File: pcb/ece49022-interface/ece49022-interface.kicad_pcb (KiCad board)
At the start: 4 copper layers, 102 x 99 mm, 30 parts, among them J1 Conn_01x02_Pin, Q1 KSC1815, U4 NCP1117-3.3_SOT223, U5 TPS54202DDCT

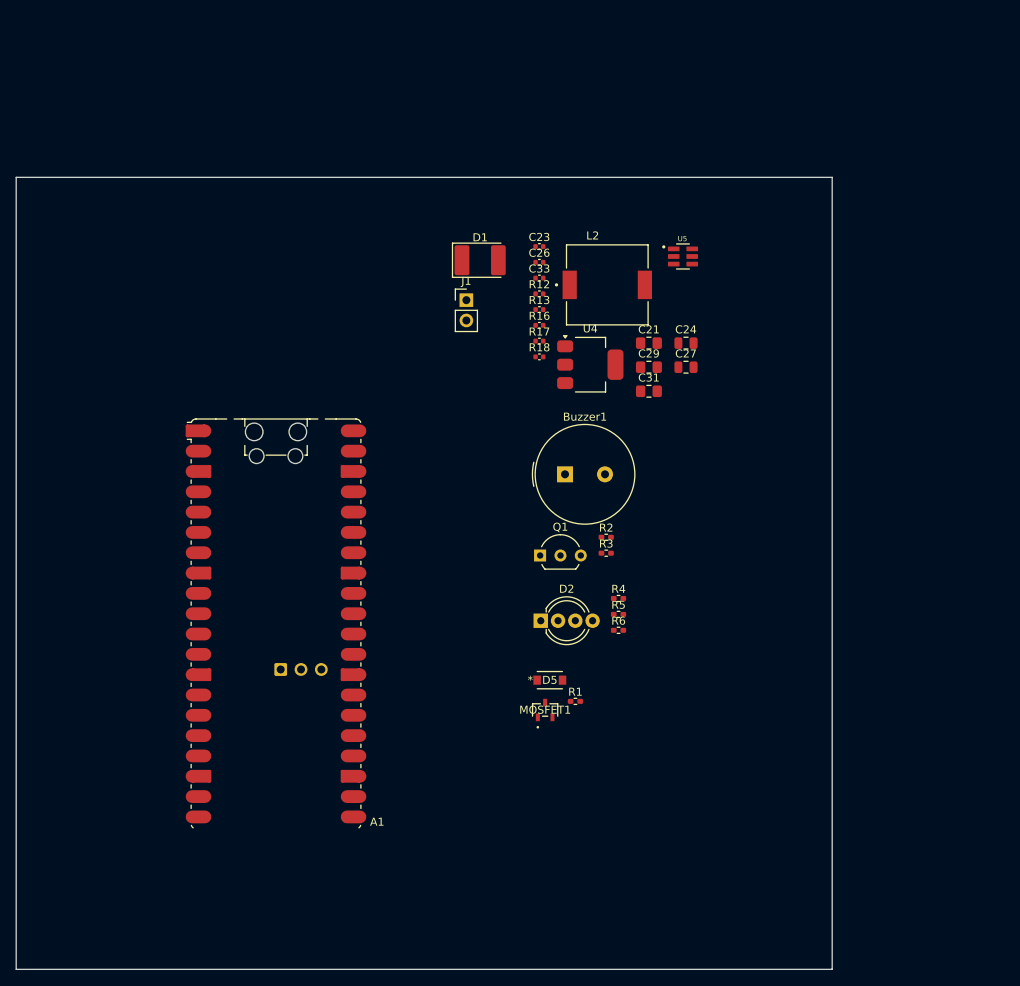
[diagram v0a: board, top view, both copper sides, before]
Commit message: Add pin connectors
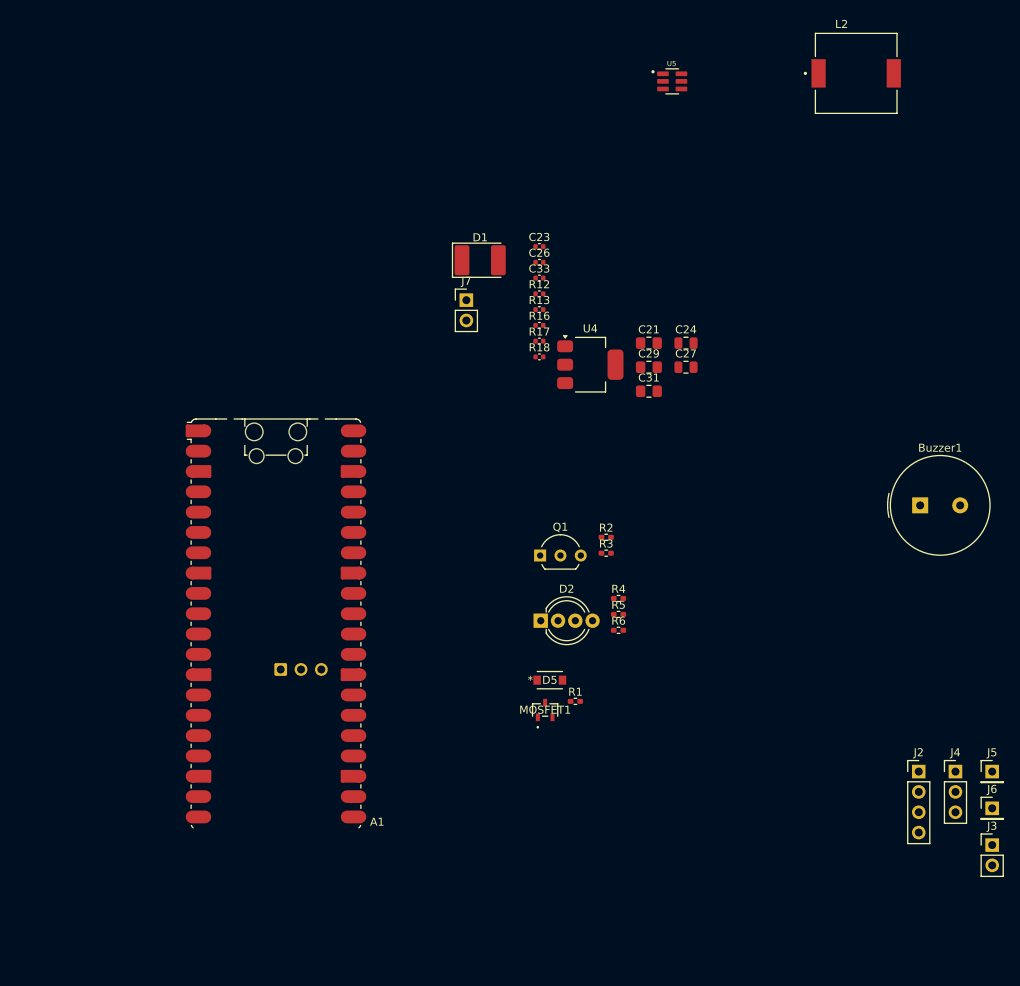
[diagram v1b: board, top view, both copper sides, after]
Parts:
- added J2: Conn_01x04_Pin, Connector_PinHeader_2.54mm:PinHeader_1x04_P2.54mm_Vertical, F.Cu at (197.8, 117.3)
- added J3: Conn_01x02_Pin, Connector_PinHeader_2.54mm:PinHeader_1x02_P2.54mm_Vertical, F.Cu at (207.0, 126.5)
- added J4: Conn_01x03_Pin, Connector_PinHeader_2.54mm:PinHeader_1x03_P2.54mm_Vertical, F.Cu at (202.4, 117.3)
- added J5: Conn_01x01_Pin, Connector_PinHeader_2.54mm:PinHeader_1x01_P2.54mm_Vertical, F.Cu at (207.0, 117.3)
- added J6: Conn_01x01_Pin, Connector_PinHeader_2.54mm:PinHeader_1x01_P2.54mm_Vertical, F.Cu at (207.0, 121.9)
- moved Buzzer1 44.6 mm to (198.0, 84.0)
- moved L2 40.8 mm to (190.0, 30.0)
- moved U5 21.9 mm to (167.0, 31.0)
- renumbered J1 to J7
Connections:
- J7 pad 2: /LOCK_RTN -> GND
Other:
- board outline removed

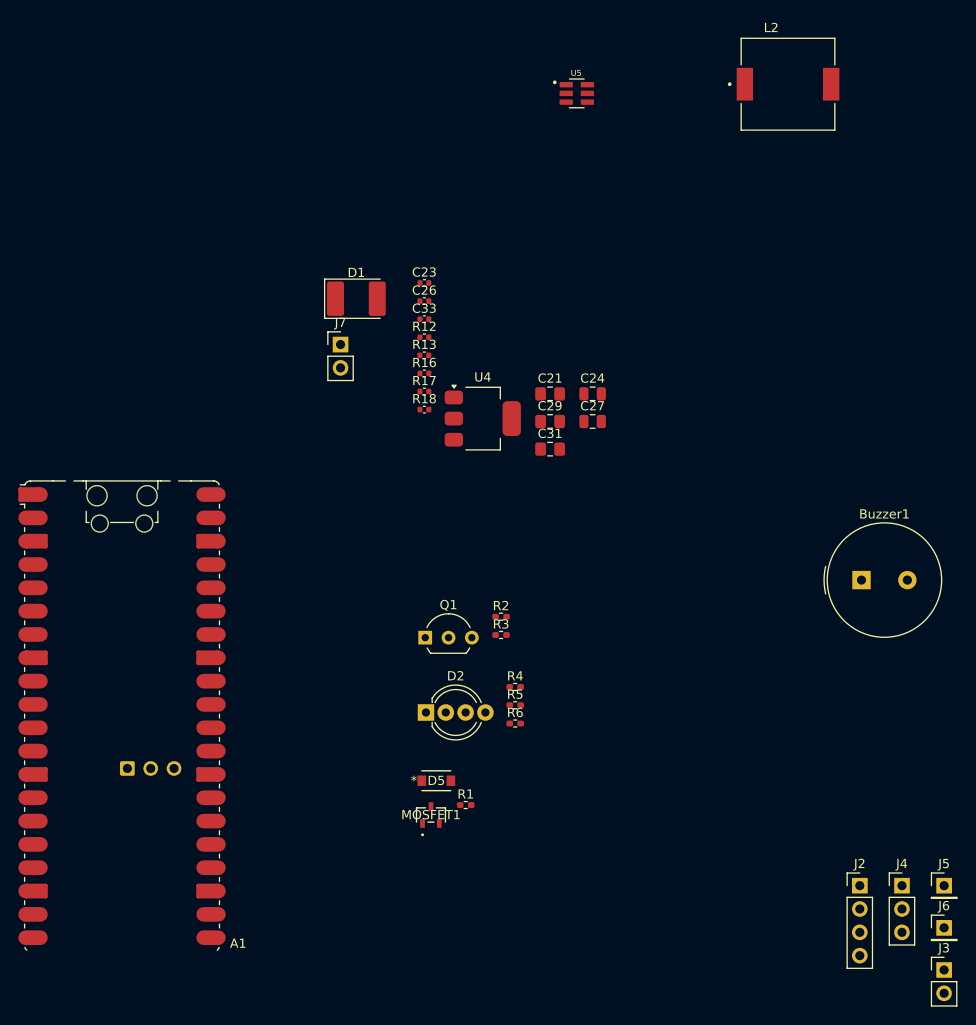
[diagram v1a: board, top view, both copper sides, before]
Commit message: Redid external pin connectors
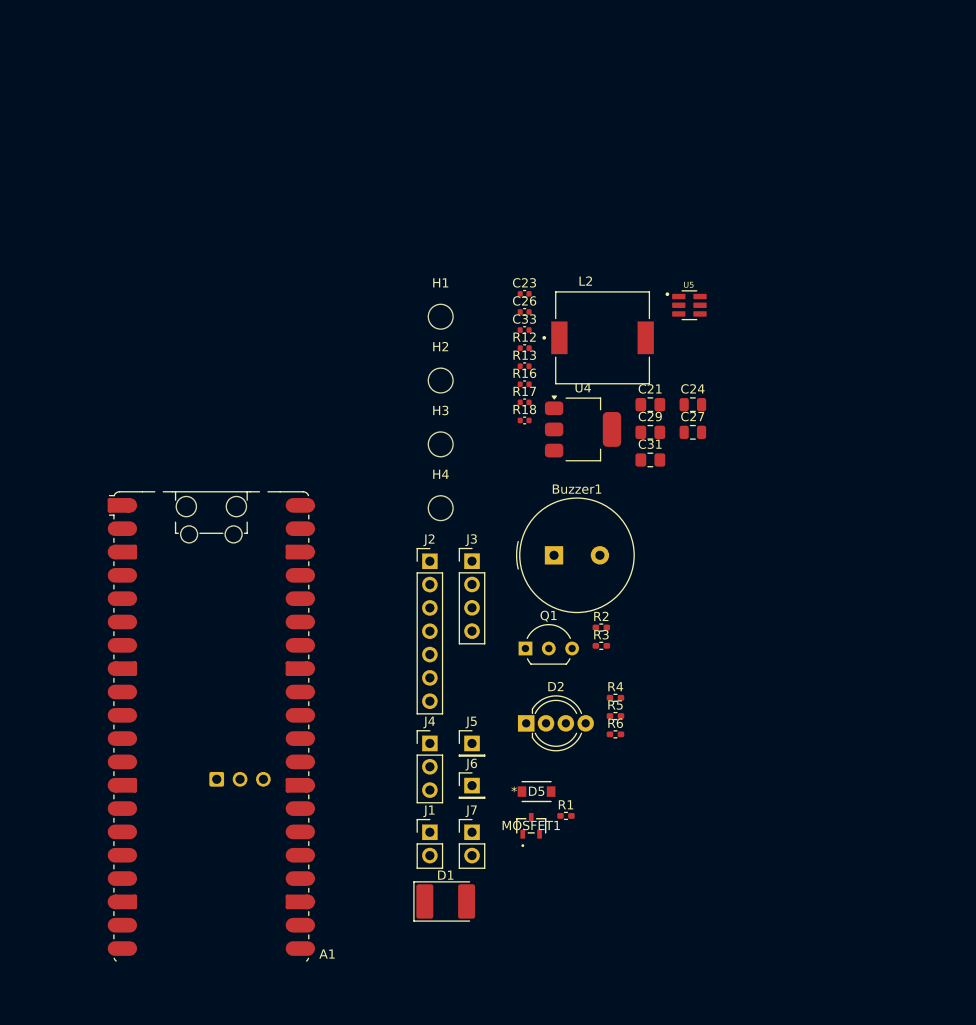
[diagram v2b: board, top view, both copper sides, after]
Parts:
- added H1: MountingHole, MountingHole:MountingHole_2.7mm_M2.5, F.Cu at (152.2, 55.3)
- added H2: MountingHole, MountingHole:MountingHole_2.7mm_M2.5, F.Cu at (152.2, 62.3)
- added H3: MountingHole, MountingHole:MountingHole_2.7mm_M2.5, F.Cu at (152.2, 69.2)
- added H4: MountingHole, MountingHole:MountingHole_2.7mm_M2.5, F.Cu at (152.2, 76.2)
- added J1: Conn_01x02_Pin, Connector_PinHeader_2.54mm:PinHeader_1x02_P2.54mm_Vertical, F.Cu at (151.0, 111.5)
- J2: value Conn_01x04_Pin -> Conn_01x07_Pin; footprint Connector_PinHeader_2.54mm:PinHeader_1x04_P2.54mm_Vertical -> Connector_PinHeader_2.54mm:PinHeader_1x07_P2.54mm_Vertical
- J3: value Conn_01x02_Pin -> Conn_01x04_Pin; footprint Connector_PinHeader_2.54mm:PinHeader_1x02_P2.54mm_Vertical -> Connector_PinHeader_2.54mm:PinHeader_1x04_P2.54mm_Vertical
- moved J3 68.0 mm to (155.6, 81.9)
- moved D1 66.4 mm to (152.7, 119.0)
- moved J2 58.7 mm to (151.0, 82.0)
- moved J7 55.0 mm to (155.6, 111.5)
- moved J4 53.7 mm to (151.0, 101.8)
- moved J5 53.7 mm to (155.6, 101.8)
- moved J6 53.7 mm to (155.6, 106.4)
- moved L2 34.2 mm to (169.8, 57.6)
- moved Buzzer1 33.6 mm to (164.5, 81.3)
- moved U5 26.1 mm to (179.3, 54.1)
- moved D2 11.0 mm to (161.5, 99.6)
- moved D5 11.0 mm to (162.6, 107.0)
- moved R4 11.0 mm to (171.2, 96.8)
- moved R5 11.0 mm to (171.2, 98.8)
- moved R6 11.0 mm to (171.2, 100.8)
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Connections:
- J2 pad 1: /BC_SCK -> GND
- J2 pad 2: /BC_Rx -> +5V
- J2 pad 3: /BC_Tx -> +3V3
- J2 pad 4: /BC_CSn -> /BC_SCK

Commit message: pcb in progress
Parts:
- removed J4: Conn_01x03_Pin, Connector_PinHeader_2.54mm:PinHeader_1x03_P2.54mm_Vertical
- removed J5, J6: Conn_01x01_Pin, Connector_PinHeader_2.54mm:PinHeader_1x01_P2.54mm_Vertical
- J1: value Conn_01x02_Pin -> Conn_01x03_Pin; footprint Connector_PinHeader_2.54mm:PinHeader_1x02_P2.54mm_Vertical -> Connector_PinHeader_2.54mm:PinHeader_1x03_P2.54mm_Vertical
- moved H3 223.8 mm to (-67.3, 25.4)
- moved H1 223.4 mm to (-67.3, 14.0)
- moved H4 216.6 mm to (-58.4, 25.4)
- moved H2 216.1 mm to (-58.4, 14.0)
- moved C23 117.1 mm to (44.7, 42.4)
- moved C26 117.1 mm to (44.7, 44.4)
- moved C33 117.1 mm to (44.7, 46.4)
- moved L2 117.1 mm to (53.2, 47.2)
- moved R12 117.1 mm to (44.7, 48.3)
- moved R13 117.1 mm to (44.7, 50.3)
- moved R16 117.1 mm to (44.7, 52.3)
- moved R17 117.1 mm to (44.7, 54.2)
- moved R18 117.1 mm to (44.7, 56.2)
- moved U4 117.1 mm to (51.1, 57.2)
- moved C21 117.1 mm to (58.4, 54.5)
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
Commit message: update for pcb
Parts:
- removed D2: LED_KRGB, LED_THT:LED_D5.0mm-4_RGB_Wide_Pins
- removed J7: Conn_01x02_Pin, Connector_PinHeader_2.54mm:PinHeader_1x02_P2.54mm_Vertical
- added J4: Conn_01x04_Pin, Connector_PinHeader_2.54mm:PinHeader_1x04_P2.54mm_Vertical, F.Cu at (114.9, 78.7)
- added J5: Conn_01x02_Pin, Connector_PinHeader_2.54mm:PinHeader_1x02_P2.54mm_Vertical, F.Cu at (189.4, 102.8)
- added J6: Conn_01x02_Pin, Connector_PinHeader_2.54mm:PinHeader_1x02_P2.54mm_Vertical, F.Cu at (114.8, 97.6)
- J2: value Conn_01x07_Pin -> Conn_01x05_Pin; footprint Connector_PinHeader_2.54mm:PinHeader_1x07_P2.54mm_Vertical -> Connector_PinHeader_2.54mm:PinHeader_1x05_P2.54mm_Vertical
- moved H4 287.8 mm to (201.1, 149.8)
- moved H2 254.6 mm to (192.3, 58.5)
- moved H3 210.6 mm to (96.6, 157.7)
- moved H1 175.0 mm to (102.4, 56.5)
- moved C23 108.6 mm to (131.0, 108.5), turned to -90 degrees
- moved R13 108.1 mm to (134.5, 110.5), turned to -90 degrees
- moved R12 108.1 mm to (134.5, 108.5), turned to -90 degrees
- moved C33 106.6 mm to (136.1, 101.3), turned to -90 degrees
- moved C26 105.9 mm to (132.7, 103.3)
- moved R18 104.3 mm to (135.7, 107.2), turned to -90 degrees
- moved R17 103.7 mm to (137.2, 101.2), turned to -90 degrees
- moved R16 102.8 mm to (136.1, 99.3), turned to -90 degrees
- moved J1 94.5 mm to (189.4, 111.7), turned to 180 degrees
- moved U5 93.6 mm to (132.8, 105.8)
- moved C21 92.5 mm to (132.7, 109.7), turned to -90 degrees
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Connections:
- A1 pad 10: /GPIO7 -> unconnected-(A1-GPIO7-Pad10)
- A1 pad 11: /GPIO8 -> unconnected-(A1-GPIO8-Pad11)
- A1 pad 16: /GPIO12 -> /BC_Rx
- A1 pad 17: unconnected-(A1-GPIO13-Pad17) -> /BC_Tx
- A1 pad 21: /GPIO16 -> /FS_Rx
- A1 pad 22: unconnected-(A1-GPIO17-Pad22) -> /FS_Tx
- A1 pad 24: unconnected-(A1-GPIO18-Pad24) -> /GPIO18
- A1 pad 26: unconnected-(A1-GPIO20-Pad26) -> /MAIN_MCU_I2C_SDA
- A1 pad 27: /FS_Rx -> /MAIN_MCU_I2C_SCL
- A1 pad 29: /FS_Tx -> /GPIO22
- A1 pad 4: /BC_SCK -> Net-(A1-GPIO2)
- A1 pad 5: /BC_Rx -> Net-(A1-GPIO3)
- A1 pad 6: /BC_Tx -> Net-(A1-GPIO4)
- A1 pad 7: /BC_CSn -> unconnected-(A1-GPIO5-Pad7)
- A1 pad 9: /GPIO6 -> unconnected-(A1-GPIO6-Pad9)
- J1 pad 3: /GPIO12 -> /GPIO18
- J2 pad 2: +5V -> +3V3
- J2 pad 3: +3V3 -> +5V
- J2 pad 4: /BC_SCK -> /BC_Rx
- J2 pad 5: /BC_Rx -> /BC_Tx
- J3 pad 1: /FS_Tx -> GND
- J3 pad 2: /FS_Rx -> +3V3
- J3 pad 3: +3V3 -> /FS_Tx
- J3 pad 4: GND -> /FS_Rx
- MOSFET1 pad 1: /GPIO12 -> /GPIO18
- R1 pad 1: /GPIO12 -> /GPIO18
- R2 pad 1: /GPIO16 -> /GPIO22
- R4 pad 1: Net-(D2-RA) -> /PWM_R
- R4 pad 2: /GPIO6 -> Net-(A1-GPIO2)
- R5 pad 1: Net-(D2-GA) -> /PWM_G
- R5 pad 2: /GPIO7 -> Net-(A1-GPIO3)
- R6 pad 1: Net-(D2-BA) -> /PWM_B
- R6 pad 2: /GPIO8 -> Net-(A1-GPIO4)

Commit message: prepared for fills
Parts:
- moved H3 33.4 mm to (118.0, 132.0)
- moved H4 22.7 mm to (187.0, 132.0)
- moved H1 16.0 mm to (118.0, 53.0)
- moved H2 7.64 mm to (187.0, 53.0)
- moved Buzzer1 6.40 mm to (176.5, 86.7), turned to 0 degrees
- moved R3 2.79 mm to (178.8, 96.7), turned to 180 degrees
- moved C21 2.59 mm to (135.3, 109.6)
- moved C23 2.59 mm to (133.6, 108.4)
- moved C24 2.59 mm to (124.8, 94.8)
- moved C26 2.59 mm to (135.3, 103.3)
- moved C27 2.59 mm to (136.8, 94.3)
- moved C29 2.59 mm to (134.4, 99.7)
- moved C31 2.59 mm to (136.8, 99.7)
- moved J2 2.59 mm to (117.4, 104.2)
- moved J6 2.59 mm to (117.4, 97.6)
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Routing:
- added copper zone on B.Cu, net GND
- added copper zone on F.Cu, net GND
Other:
- board outline added: 80 x 90 mm

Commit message: final layout i think
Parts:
- moved C21 35.2 mm to (141.5, 75.0)
- moved C23 35.2 mm to (139.8, 73.8)
- moved C29 35.2 mm to (140.6, 65.0)
- moved C31 35.2 mm to (143.0, 65.0)
- moved C33 35.2 mm to (144.9, 66.6)
- moved L2 35.2 mm to (133.6, 68.8)
- moved R12 35.2 mm to (143.3, 73.8)
- moved R13 35.2 mm to (143.3, 75.8)
- moved R16 35.2 mm to (144.9, 64.6)
- moved R17 35.2 mm to (146.0, 66.5)
- moved R18 35.2 mm to (144.5, 72.5)
- moved U4 35.2 mm to (136.8, 58.8)
- moved U5 35.2 mm to (141.6, 71.0)
- moved C24 35.2 mm to (131.0, 60.1)
- moved C27 35.2 mm to (143.0, 59.6)
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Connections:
- A1 pad 10: unconnected-(A1-GPIO7-Pad10) -> Net-(A1-GPIO7)
- A1 pad 11: unconnected-(A1-GPIO8-Pad11) -> Net-(A1-GPIO8)
- A1 pad 4: Net-(A1-GPIO2) -> unconnected-(A1-GPIO2-Pad4)
- A1 pad 5: Net-(A1-GPIO3) -> unconnected-(A1-GPIO3-Pad5)
- A1 pad 6: Net-(A1-GPIO4) -> unconnected-(A1-GPIO4-Pad6)
- A1 pad 9: unconnected-(A1-GPIO6-Pad9) -> Net-(A1-GPIO6)
- R4 pad 2: Net-(A1-GPIO2) -> Net-(A1-GPIO6)
- R5 pad 2: Net-(A1-GPIO3) -> Net-(A1-GPIO7)
- R6 pad 2: Net-(A1-GPIO4) -> Net-(A1-GPIO8)
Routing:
- added copper zone on F.Cu, net +3V3
- removed copper zone on B.Cu, net GND
- removed copper zone on F.Cu, net GND
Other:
- board size 80 x 90 mm -> 63.3 x 77 mm

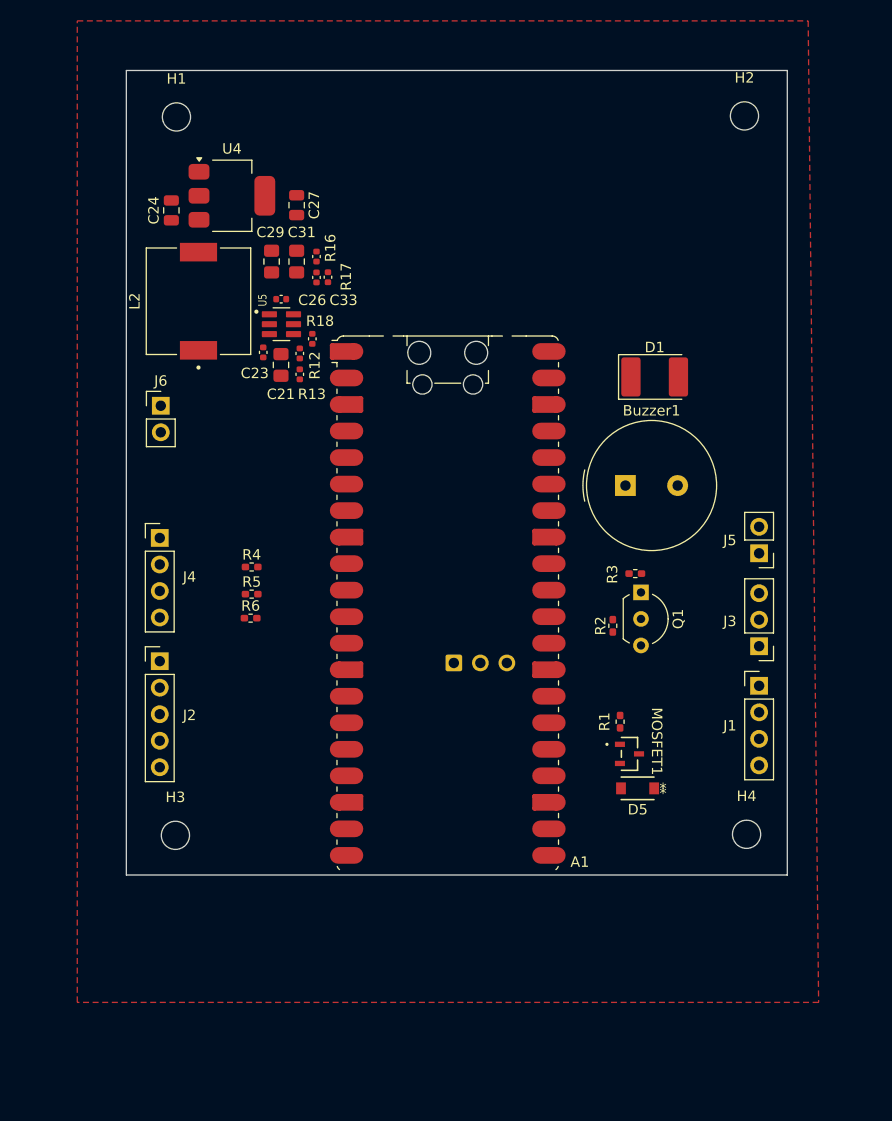
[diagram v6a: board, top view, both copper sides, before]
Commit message: need to add traces
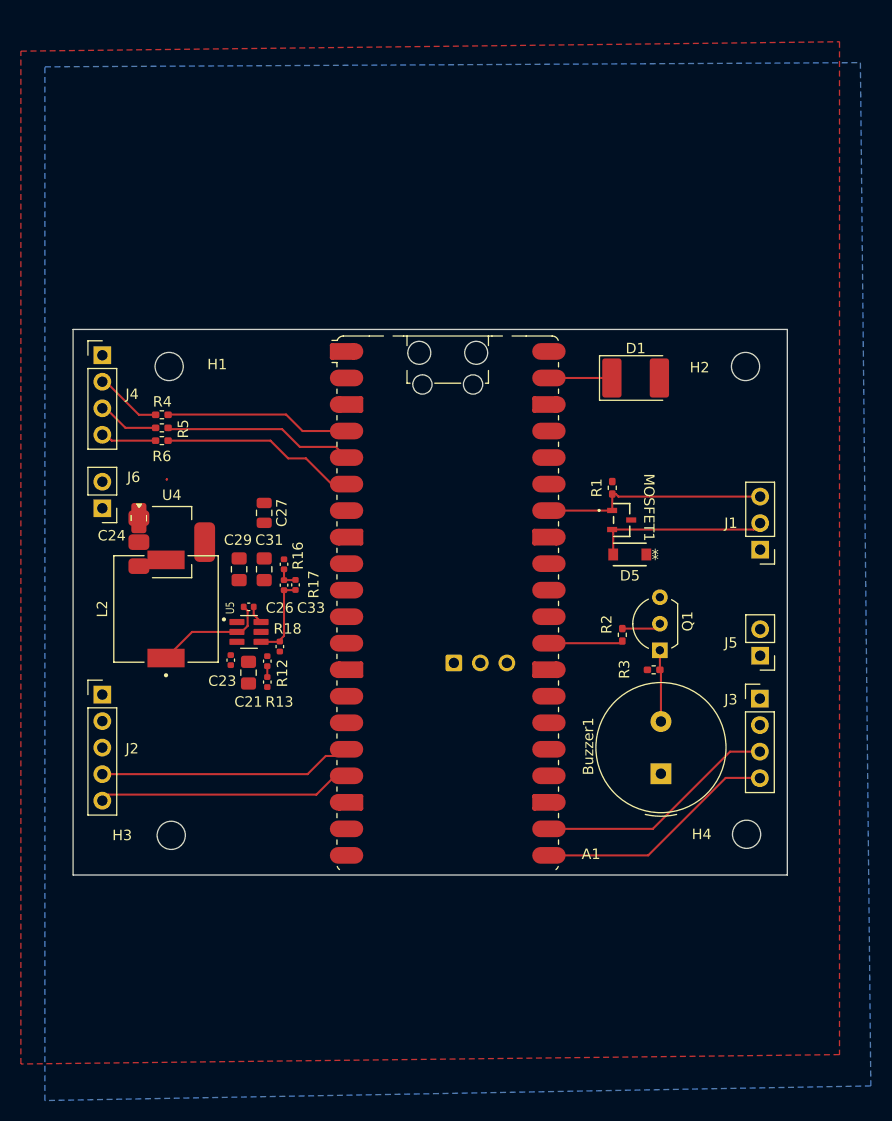
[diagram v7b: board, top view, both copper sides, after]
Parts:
- moved U4 33.7 mm to (131.1, 91.9)
- moved C33 29.6 mm to (141.8, 96.0)
- moved R16 29.6 mm to (141.8, 94.0)
- moved C23 29.6 mm to (136.7, 103.2)
- moved C24 29.6 mm to (127.9, 89.6)
- moved C26 29.6 mm to (138.4, 98.1)
- moved C27 29.6 mm to (139.9, 89.1)
- moved C29 29.6 mm to (137.5, 94.5)
- moved L2 29.6 mm to (130.5, 98.3)
- moved R12 29.6 mm to (140.2, 103.3)
- moved R13 29.6 mm to (140.2, 105.3)
- moved U5 29.6 mm to (138.4, 100.5)
- moved C21 29.6 mm to (138.4, 104.4)
- moved C31 29.6 mm to (139.9, 94.5)
- moved R17 29.6 mm to (142.9, 96.0)
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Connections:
- A1 pad 10: Net-(A1-GPIO7) -> unconnected-(A1-GPIO7-Pad10)
- A1 pad 11: Net-(A1-GPIO8) -> unconnected-(A1-GPIO8-Pad11)
- A1 pad 24: /GPIO18 -> unconnected-(A1-GPIO18-Pad24)
- A1 pad 34: unconnected-(A1-GPIO28_ADC2-Pad34) -> /GPIO28
- A1 pad 4: unconnected-(A1-GPIO2-Pad4) -> Net-(A1-GPIO2)
- A1 pad 5: unconnected-(A1-GPIO3-Pad5) -> Net-(A1-GPIO3)
- A1 pad 6: unconnected-(A1-GPIO4-Pad6) -> Net-(A1-GPIO4)
- A1 pad 9: Net-(A1-GPIO6) -> unconnected-(A1-GPIO6-Pad9)
- J1 pad 3: /GPIO18 -> /GPIO28
- MOSFET1 pad 1: /GPIO18 -> /GPIO28
- R1 pad 1: /GPIO18 -> /GPIO28
- R4 pad 2: Net-(A1-GPIO6) -> Net-(A1-GPIO2)
- R5 pad 2: Net-(A1-GPIO7) -> Net-(A1-GPIO3)
- R6 pad 2: Net-(A1-GPIO8) -> Net-(A1-GPIO4)
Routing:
- net /BC_Tx: track 0.00 -> 24.4 mm
- net /BC_Rx: track 0.00 -> 24.4 mm
- net /FS_Rx: track 0.00 -> 23.3 mm
- net /FS_Tx: track 0.00 -> 23.3 mm
- net /GPIO28: track 0.00 -> 21.9 mm
- net Net-(A1-GPIO4): track 0.00 -> 18.8 mm
- net Net-(A1-GPIO3): track 0.00 -> 18.5 mm
- net Net-(A1-GPIO2): track 0.00 -> 17.8 mm
- net /LOCK_RTN: track 0.00 -> 16.9 mm
- net Net-(U5-SW): track 0.00 -> 11.1 mm
- net /Power/FB: track 0.00 -> 8.01 mm
- net /GPIO22: track 0.00 -> 7.11 mm
- net Net-(Q1-C): track 0.00 -> 6.87 mm
- net /PWM_R: track 0.00 -> 6.70 mm
- net /PWM_G: track 0.00 -> 6.16 mm
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- added copper zone on B.Cu, net +3V3
- added copper zone on F.Cu, net +5V
- added copper zone on In1.Cu, net GND
- added copper zone on In2.Cu, net GND
- removed copper zone on F.Cu, net +3V3
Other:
- board size 63.3 x 77 mm -> 68.4 x 52.2 mm
